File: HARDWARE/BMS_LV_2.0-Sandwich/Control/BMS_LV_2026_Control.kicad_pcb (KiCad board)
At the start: 6 copper layers, 62.5 x 36.4 mm, 63 parts, among them IC1 TAR5S33UTE85LF, IC4 TPS54202HDDCR, J1 Conn_01x26, J3 FTSH-107-01-L-D-K, U1 STM32G484RETx, U7 ADM3057ExRW, Y1 ATX-11-F-32.000MHZ-F05-T

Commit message: Ulozono silkscreena
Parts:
- removed C33: 100n, Capacitor_SMD:C_0603_1608Metric_Pad1.08x0.95mm_HandSolder
- added C25: 100nF, Capacitor_SMD:C_0603_1608Metric, F.Cu at (144.8, 116.5)
- added C27: 100nF, Capacitor_SMD:C_0603_1608Metric, F.Cu at (147.8, 116.5)
- added C44: 100nF, Capacitor_SMD:C_0603_1608Metric, F.Cu at (150.8, 114.8)
- added C50: 100nF, Capacitor_SMD:C_0603_1608Metric, F.Cu at (153.8, 114.8)
- added C51: 100nF, Capacitor_SMD:C_0603_1608Metric, F.Cu at (156.8, 114.8)
- added C54: 100nF, Capacitor_SMD:C_0603_1608Metric, F.Cu at (159.8, 114.8)
- added C55: 100nF, Capacitor_SMD:C_0603_1608Metric, F.Cu at (162.8, 114.8)
- added C56: 100nF, Capacitor_SMD:C_0603_1608Metric, F.Cu at (178.7, 115.7)
- added C57: 22u, Capacitor_SMD:C_0805_2012Metric_Pad1.18x1.45mm_HandSolder, F.Cu at (182.9, 97.1)
- added C58: 100n, Capacitor_SMD:C_0603_1608Metric, F.Cu at (186.2, 100.0)
- added C59: 22u, Capacitor_SMD:C_0805_2012Metric_Pad1.18x1.45mm_HandSolder, F.Cu at (189.0, 98.8)
- added C60: 100n, Capacitor_SMD:C_0603_1608Metric_Pad1.08x0.95mm_HandSolder, F.Cu at (160.6, 97.5)
- added C61: 100n, Capacitor_SMD:C_0603_1608Metric_Pad1.08x0.95mm_HandSolder, F.Cu at (159.1, 97.5)
- added D18: ~, LED_SMD:LED_0603_1608Metric_Pad1.05x0.95mm_HandSolder, F.Cu at (159.7, 88.0)
- added F6: SMDH2920B150TF, Fuse:Fuse_2920_7451Metric_Pad2.10x5.45mm_HandSolder, F.Cu at (188.5, 85.5)
- added IC2: TAR5S33UTE85LF, Footprint:SOTFL65P210X75-5N, F.Cu at (186.3, 97.9)
- added J6: Conn_01x09_Female, Footprint:S9BXHA1LFSN, B.Cu at (152.2, 118.5)
- added R18: 100, Resistor_SMD:R_0603_1608Metric_Pad0.98x0.95mm_HandSolder, F.Cu at (156.4, 88.0)
- added R51: 10k, Resistor_SMD:R_0603_1608Metric, F.Cu at (146.2, 116.5)
- added R52: 10k, Resistor_SMD:R_0603_1608Metric, F.Cu at (149.2, 116.5)
- added R53: 10k, Resistor_SMD:R_0603_1608Metric, F.Cu at (152.2, 114.8)
- added R54: 10k, Resistor_SMD:R_0603_1608Metric, F.Cu at (155.2, 114.8)
- added R55: 10k, Resistor_SMD:R_0603_1608Metric, F.Cu at (158.2, 114.8)
- added R56: 10k, Resistor_SMD:R_0603_1608Metric, F.Cu at (161.2, 114.8)
- added R63: 10k, Resistor_SMD:R_0603_1608Metric, F.Cu at (164.2, 114.8)
- added R64: 10k, Resistor_SMD:R_0603_1608Metric, F.Cu at (177.2, 115.8)
- D7, D8: moved to B.Cu
- F3, F4, F5: moved to F.Cu
- moved C53 46.8 mm to (156.0, 112.3)
- moved R28 41.7 mm to (143.2, 105.0), turned to 90 degrees
- moved C29 40.3 mm to (144.5, 107.5), turned to 0 degrees
- moved C31 40.1 mm to (186.5, 95.8), turned to 0 degrees
- moved C45 39.4 mm to (188.8, 92.8), turned to -90 degrees
- moved Y1 39.2 mm to (160.5, 109.8), turned to 180 degrees
- moved C46 36.4 mm to (184.0, 93.2), turned to 90 degrees
- moved C47 36.4 mm to (185.9, 113.3)
- moved FB7 35.5 mm to (186.8, 110.5), turned to 0 degrees
- moved IC1 35.4 mm to (186.2, 93.2), turned to 90 degrees
- moved FB8 33.7 mm to (186.8, 108.8), turned to 0 degrees
- moved C52 33.6 mm to (164.1, 109.9), turned to 90 degrees
- moved FB6 32.8 mm to (172.3, 114.8), turned to 180 degrees
- moved U1 32.7 mm to (151.5, 102.5), turned to 90 degrees
- moved C34 32.5 mm to (156.5, 109.5), turned to 90 degrees
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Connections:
- D7 pad 3: /Control/SWO -> unconnected-(D7-I/O2-Pad3)
- D7 pad 4: /Control/SWCLK -> /Control/SWDIO
- D7 pad 6: /Control/SWDIO -> /Control/SWCLK
- J1 pad 10: /Therm_6 -> unconnected-(J1-Pin_10-Pad10)
- J1 pad 11: /Therm_7 -> unconnected-(J1-Pin_11-Pad11)
- J1 pad 12: /Therm_8 -> unconnected-(J1-Pin_12-Pad12)
- J1 pad 5: /Therm_1 -> unconnected-(J1-Pin_5-Pad5)
- J1 pad 6: /Therm_2 -> unconnected-(J1-Pin_6-Pad6)
- J1 pad 7: /Therm_3 -> unconnected-(J1-Pin_7-Pad7)
- J1 pad 8: /Therm_4 -> unconnected-(J1-Pin_8-Pad8)
- J1 pad 9: /Therm_5 -> unconnected-(J1-Pin_9-Pad9)
- R25 pad 2: /3V3 -> /3V3A
- R28 pad 2: /Control/NRST -> Net-(U1-PB8)
- U1 pad 10: /Therm_8 -> /Therm_6
- U1 pad 17: /Therm_4 -> /Therm_7
- U1 pad 29: /3V3 -> /3V3A
- U1 pad 36: /Therm_5 -> /Therm_8
- U1 pad 61: /Control/NRST -> Net-(U1-PB8)
- U1 pad 7: unconnected-(U1-PG10-Pad7) -> /Control/NRST
- U1 pad 8: /Therm_6 -> /Therm_4
- U1 pad 9: /Therm_7 -> /Therm_5
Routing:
- net /3V3A: track 0.00 -> 128.3 mm, vias 0 -> 6
- net /Control/URAT_RX: track 54.8 -> 17.9 mm, vias 3 -> 1
- net /Switch_Signal: track 54.9 -> 19.8 mm, vias 3 -> 2
- net /SPI.CS: track 44.4 -> 10.1 mm, vias 2 -> 1
- net /VoltageFuseMeasure: track 50.4 -> 17.5 mm
- net /CAN+: track 26.9 -> 59.0 mm, vias 2 -> 1
- net /Therm_8: track 14.3 -> 44.1 mm, vias 2 -> 1
- net /CAN-: track 26.9 -> 56.0 mm, vias 2 -> 1
- net GND: track 92.0 -> 63.6 mm, vias 36 -> 59
- net /Control/URAT_TX: track 48.3 -> 20.8 mm, vias 3 -> 1
- net Net-(D16-A): track 26.6 -> 4.15 mm, vias 1 -> 0
- net /Control/SWDIO: track 41.3 -> 20.8 mm, vias 3 -> 1
- net /SPI.SCK: track 43.7 -> 24.0 mm
- net /Control/SWCLK: track 44.5 -> 26.3 mm, vias 3 -> 1
- net /USB1.USB_DP: track 36.8 -> 20.4 mm
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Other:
- board size 62.5 x 36.4 mm -> 62.5 x 40.8 mm
- board text added: "24V"
- board text added: "3.3V"
- board text added: "3V3A"
- board text added: "5V"
- board text added: "BMS LV CONTROL 2026"
- board text added: "BMS SANDWICH 2026 By Wiktor Krakowski V2.0 :P"
- board text added: "Cwel jesteś"

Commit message: Sync
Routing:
- net /CAN-: track 56.0 -> 58.4 mm
- net /3V3A: track 128.3 -> 130.5 mm
- net GND: vias 59 -> 60

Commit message: V1.0 ready for release
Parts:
- added G***: LOGO, Footprint:kmwtw2, F.Cu at (177.0, 98.5)
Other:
- board text added: "BMS SANDWICH 2026 By Wiktor Krakowski V1.0"
- board text added: "ISO CAN FD"
- board text added: "MCU"
- board text added: "POWER"
- board text added: "STATUS"
- board text added: "THERM"
- board text removed: "BMS SANDWICH 2026 By Wiktor Krakowski V2.0 :P"

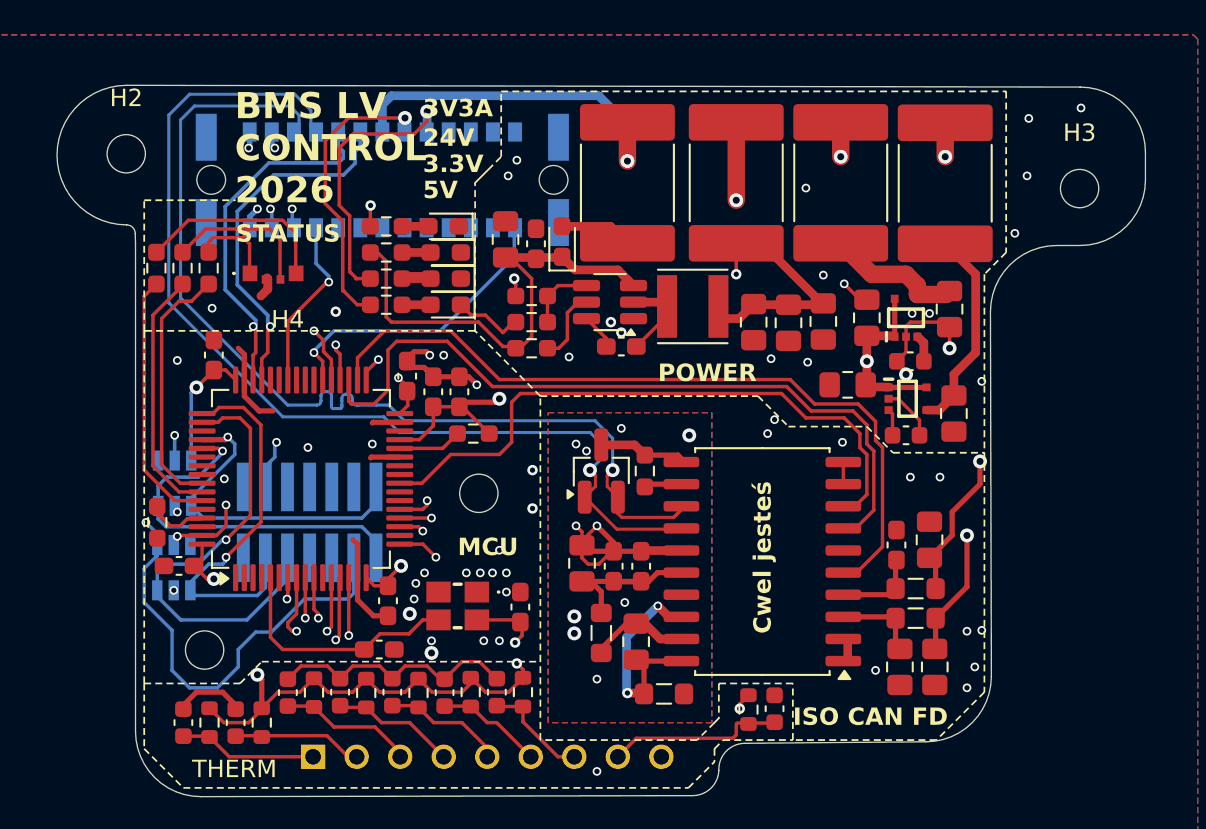
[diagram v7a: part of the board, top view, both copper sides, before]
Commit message: Kicad 10 sync, some silkscreen changes
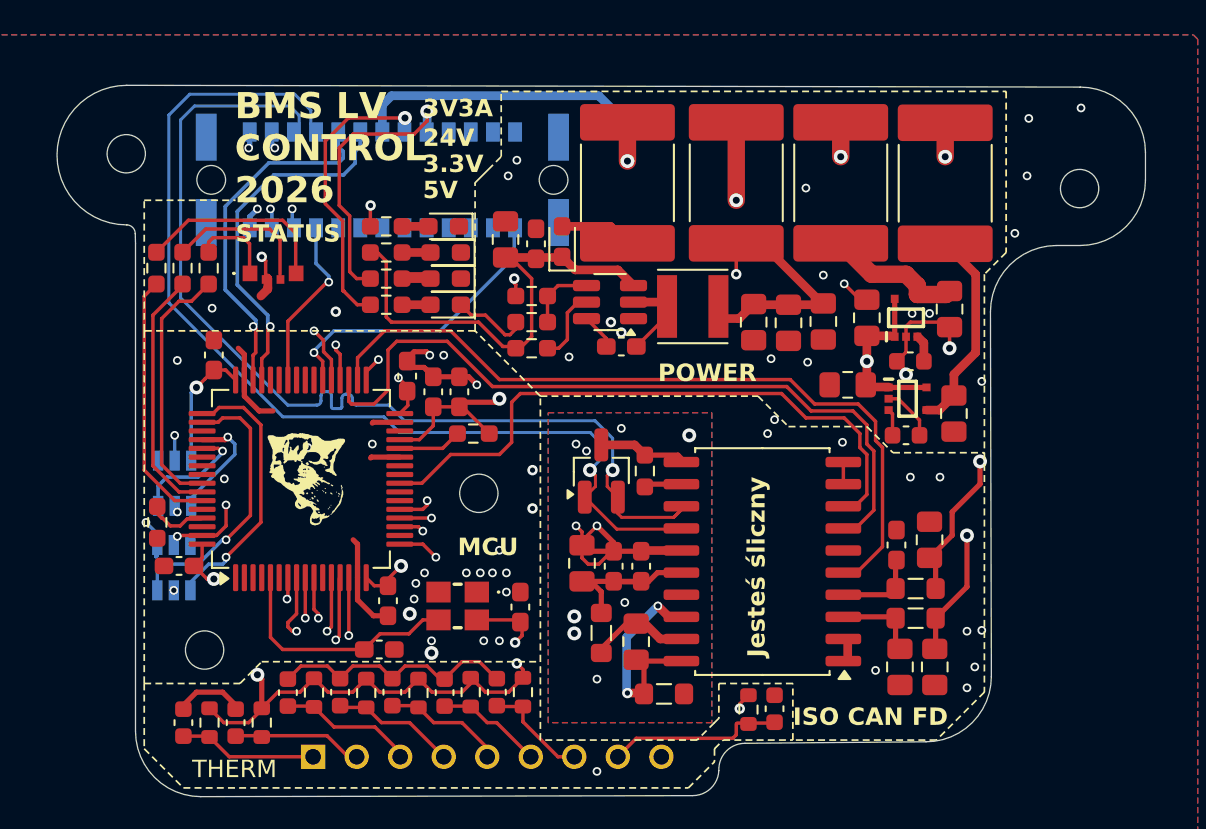
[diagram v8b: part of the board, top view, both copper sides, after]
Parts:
- removed J3: FTSH-107-01-L-D-K, Footprint:FTSH-107-XX-YYY-DV-K
- added G***: LOGO, Footprint:8x8cat_neg, F.Cu at (151.2, 103.0)
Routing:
- net /Control/NRST: track 38.6 -> 15.3 mm
- net /Control/URAT_TX: track 20.8 -> 6.97 mm
- net /Control/URAT_RX: track 17.9 -> 6.24 mm
- net /Control/SWCLK: track 26.3 -> 15.9 mm
- net /Control/SWDIO: track 20.8 -> 14.5 mm
- net /3V3: track 46.8 -> 44.7 mm, vias 9 -> 8
- net GND: track 63.6 -> 65.2 mm, vias 60 -> 61
- net /Power/SW_+5V: track 5.06 -> 4.17 mm
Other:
- board text added: "Jesteś śliczny"
- board text removed: "Cwel jesteś"
